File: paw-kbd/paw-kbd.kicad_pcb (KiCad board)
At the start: 2 copper layers, 30 parts, among them J1 OLED, J2 MJ-4PP-9, SW10 SW_PUSH, SW11 SW_PUSH, SW12 SW_PUSH, SW13 SW_PUSH, SW14 SW_PUSH, SW15 SW_PUSH, SW16 SW_PUSH, SW17 SW_PUSH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

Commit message: schematic
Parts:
- removed D14: DIODE, kbd:D3_TH_SMD
- SW1: renamed from SW4; footprint fp:ChocV1_V2_Hotswap_reversed_choc_spacing -> keeb-footprints:ChocV1_V2_Hotswap_reversed_choc_spacing
- SW10: renamed from SW13; footprint fp:ChocV1_V2_Hotswap_reversed_choc_spacing -> keeb-footprints:ChocV1_V2_Hotswap_reversed_choc_spacing
- SW11: renamed from SW14; footprint fp:ChocV1_V2_Hotswap_reversed_choc_spacing -> keeb-footprints:ChocV1_V2_Hotswap_reversed_choc_spacing
- SW12: renamed from SW15; footprint fp:ChocV1_V2_Hotswap_reversed_choc_spacing -> keeb-footprints:ChocV1_V2_Hotswap_reversed_choc_spacing
- SW13: renamed from SW16; footprint fp:ChocV1_V2_Hotswap_reversed_choc_spacing -> keeb-footprints:ChocV1_V2_Hotswap_reversed_choc_spacing
- SW14: renamed from SW17; footprint fp:ChocV1_V2_Hotswap_reversed_choc_spacing -> keeb-footprints:ChocV1_V2_Hotswap_reversed_choc_spacing
- SW15: renamed from SW18; footprint fp:ChocV1_V2_Hotswap_reversed_choc_spacing -> keeb-footprints:ChocV1_V2_Hotswap_reversed_choc_spacing
- SW2: renamed from SW5; footprint fp:ChocV1_V2_Hotswap_reversed_choc_spacing -> keeb-footprints:ChocV1_V2_Hotswap_reversed_choc_spacing
- SW3: renamed from SW6; footprint fp:ChocV1_V2_Hotswap_reversed_choc_spacing -> keeb-footprints:ChocV1_V2_Hotswap_reversed_choc_spacing
- SW4: renamed from SW7; footprint fp:ChocV1_V2_Hotswap_reversed_choc_spacing -> keeb-footprints:ChocV1_V2_Hotswap_reversed_choc_spacing
- SW5: renamed from SW8; footprint fp:ChocV1_V2_Hotswap_reversed_choc_spacing -> keeb-footprints:ChocV1_V2_Hotswap_reversed_choc_spacing
- SW6: renamed from SW9; footprint fp:ChocV1_V2_Hotswap_reversed_choc_spacing -> keeb-footprints:ChocV1_V2_Hotswap_reversed_choc_spacing
- SW7: renamed from SW10; footprint fp:ChocV1_V2_Hotswap_reversed_choc_spacing -> keeb-footprints:ChocV1_V2_Hotswap_reversed_choc_spacing
- SW8: renamed from SW11; footprint fp:ChocV1_V2_Hotswap_reversed_choc_spacing -> keeb-footprints:ChocV1_V2_Hotswap_reversed_choc_spacing
- SW9: renamed from SW12; footprint fp:ChocV1_V2_Hotswap_reversed_choc_spacing -> keeb-footprints:ChocV1_V2_Hotswap_reversed_choc_spacing
- moved J2 10.9 mm to (203.8, 102.5), turned to -90 degrees
- moved SW4 10.7 mm to (116.7, 64.9), turned to 6 degrees
- moved SW10 10.6 mm to (157.2, 64.0), turned to 0 degrees
- moved SW13 10.6 mm to (175.3, 64.0), turned to 0 degrees
- moved SW7 10.6 mm to (136.8, 61.0), turned to 3 degrees
- moved U1 10.5 mm to (194.1, 75.9), turned to 0 degrees
- moved SW5 9.78 mm to (118.5, 82.0), turned to 6 degrees
- moved SW11 9.75 mm to (157.2, 81.1), turned to 0 degrees
- moved SW14 9.70 mm to (175.3, 81.1), turned to 0 degrees
- moved SW8 9.67 mm to (137.7, 78.2), turned to 3 degrees
- moved JP4 9.65 mm to (197.0, 91.6), turned to -90 degrees
- moved JP5 9.65 mm to (197.0, 91.6), turned to -90 degrees
- moved JP3 9.64 mm to (195.1, 91.6), turned to -90 degrees
- moved JP6 9.64 mm to (195.1, 91.6), turned to -90 degrees
- moved JP2 9.63 mm to (193.2, 91.6), turned to -90 degrees
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- renumbered JP4 to JP1, JP3 to JP2, JP2 to JP3, JP1 to JP4, SW22 to SW16, SW22 to SW17

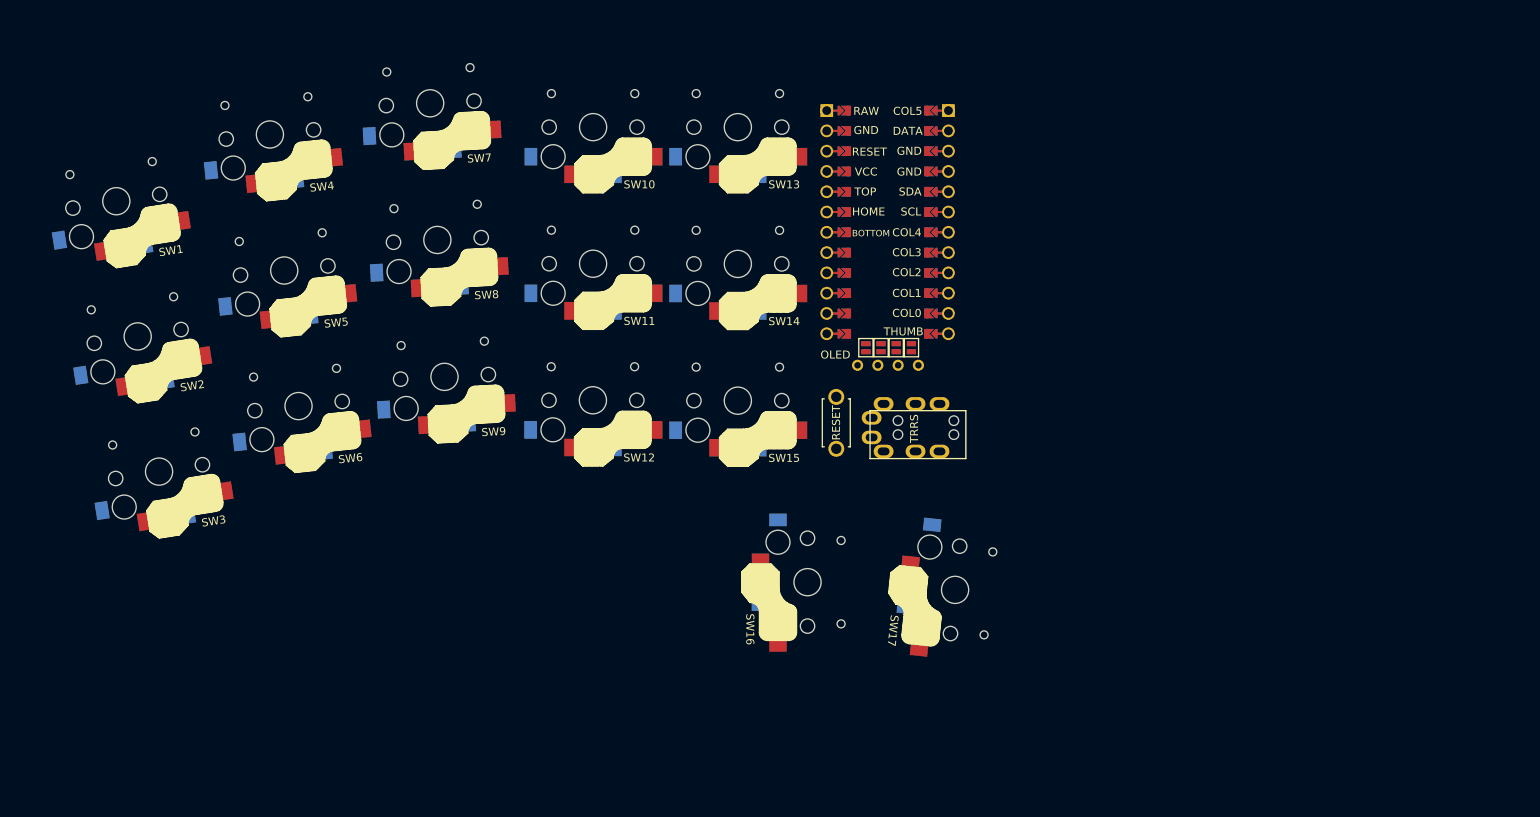
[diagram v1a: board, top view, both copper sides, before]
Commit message: optional socketed footprints
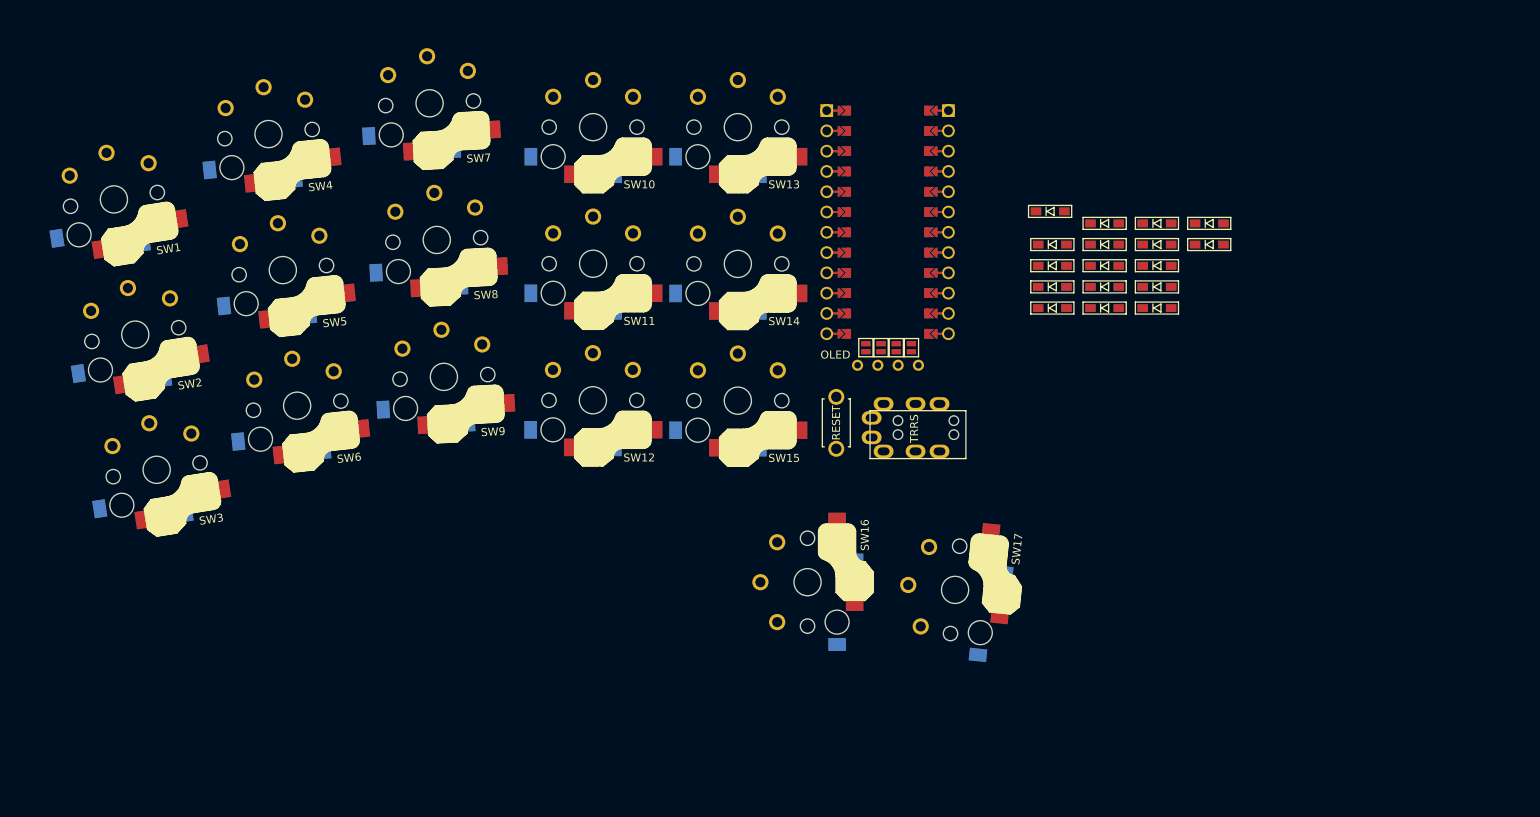
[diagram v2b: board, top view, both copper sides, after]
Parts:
- added D1: DIODE, keeb-footprints:D3_SMD, F.Cu at (214.7, 78.7)
- added D10: DIODE, keeb-footprints:D3_SMD, F.Cu at (214.7, 86.7)
- added D11: DIODE, keeb-footprints:D3_SMD, F.Cu at (221.2, 86.7)
- added D12: DIODE, keeb-footprints:D3_SMD, F.Cu at (227.8, 81.4)
- added D13: DIODE, keeb-footprints:D3_SMD, F.Cu at (227.8, 84.0)
- added D14: DIODE, keeb-footprints:D3_SMD, F.Cu at (221.2, 84.0)
- added D15: DIODE, keeb-footprints:D3_SMD, F.Cu at (234.3, 76.1)
- added D16: DIODE, keeb-footprints:D3_SMD, F.Cu at (227.8, 86.7)
- added D17: DIODE, keeb-footprints:D3_SMD, F.Cu at (227.8, 76.1)
- added D2: DIODE, keeb-footprints:D3_SMD, F.Cu at (214.7, 84.0)
- added D3: DIODE, keeb-footprints:D3_SMD, F.Cu at (234.3, 78.7)
- added D4: DIODE, keeb-footprints:D3_SMD, F.Cu at (221.2, 78.7)
- added D5: DIODE, keeb-footprints:D3_SMD, F.Cu at (214.4, 74.6)
- added D6: DIODE, keeb-footprints:D3_SMD, F.Cu at (221.2, 81.4)
- added D7: DIODE, keeb-footprints:D3_SMD, F.Cu at (227.8, 78.7)
- added D8: DIODE, keeb-footprints:D3_SMD, F.Cu at (221.2, 76.1)
- added D9: DIODE, keeb-footprints:D3_SMD, F.Cu at (214.7, 81.4)
- SW1, SW10, SW11, SW12, SW13, SW14, SW15, SW2, SW3, SW4, SW5, SW6, SW7, SW8, SW9: footprint keeb-footprints:ChocV1_V2_Hotswap_reversed_choc_spacing -> keeb-footprints:ChocV1_V2_Hotswap_optional_reversed_choc_spacing
- SW16, SW17: footprint fp:ChocV1_V2_Hotswap_reversed_15u_choc_spacing -> keeb-footprints:ChocV1_V2_Hotswap_optional_reversed_15u_choc_spacing
- U1: footprint fp:ProMicro_unrouted_type_c -> keeb-footprints:ProMicro_unrouted_type_c
- moved SW3 0.38 mm to (102.5, 106.9)
- moved SW2 0.38 mm to (99.8, 90.0)
- moved SW1 0.38 mm to (97.2, 73.1)
- moved SW4 0.18 mm to (116.5, 64.9)
- moved SW5 0.18 mm to (118.3, 81.9)
- moved SW6 0.18 mm to (120.1, 98.9)
- moved SW7 0.07 mm to (136.7, 61.0)
- moved SW8 0.07 mm to (137.6, 78.2)
- moved SW9 0.07 mm to (138.5, 95.3)
- turned SW16 to 90 degrees
- turned SW17 to 84 degrees
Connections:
- J1 pad 1: (no net) -> Net-(J1-Pad1)
- J1 pad 2: (no net) -> Net-(J1-Pad2)
- J1 pad 3: (no net) -> Net-(J1-Pad3)
- J1 pad 4: (no net) -> Net-(J1-Pad4)
- J2 pad A: (no net) -> GND
- J2 pad B: (no net) -> GND
- J2 pad C: (no net) -> data
- J2 pad D: (no net) -> VCC
- JP1 pad 1: (no net) -> GND
- JP1 pad 2: (no net) -> Net-(J1-Pad4)
- JP2 pad 1: (no net) -> VCC
- JP2 pad 2: (no net) -> Net-(J1-Pad3)
- JP3 pad 1: (no net) -> SCL
- JP3 pad 2: (no net) -> Net-(J1-Pad2)
- JP4 pad 1: (no net) -> SDA
- JP4 pad 2: (no net) -> Net-(J1-Pad1)
- JP5 pad 1: (no net) -> SDA
- JP5 pad 2: (no net) -> Net-(J1-Pad4)
- JP6 pad 1: (no net) -> SCL
- JP6 pad 2: (no net) -> Net-(J1-Pad3)
- JP7 pad 1: (no net) -> VCC
- JP7 pad 2: (no net) -> Net-(J1-Pad2)
- JP8 pad 1: (no net) -> GND
- JP8 pad 2: (no net) -> Net-(J1-Pad1)
- RSW1 pad 1: (no net) -> reset
- RSW1 pad 2: (no net) -> GND
- SW1 pad 1: (no net) -> col1
- SW1 pad 2: (no net) -> Net-(D1-Pad1)
- SW10 pad 1: (no net) -> col4
- SW10 pad 2: (no net) -> Net-(D10-Pad1)
- SW11 pad 1: (no net) -> col4
- SW11 pad 2: (no net) -> Net-(D11-Pad1)
- SW12 pad 1: (no net) -> col4
- SW12 pad 2: (no net) -> Net-(D12-Pad1)
- SW13 pad 1: (no net) -> col5
- SW13 pad 2: (no net) -> Net-(D13-Pad1)
- SW14 pad 1: (no net) -> col5
- SW14 pad 2: (no net) -> Net-(D14-Pad1)
- SW15 pad 1: (no net) -> col5
- SW15 pad 2: (no net) -> Net-(D15-Pad1)
- SW16 pad 1: (no net) -> col4
- SW16 pad 2: (no net) -> Net-(D16-Pad1)
- SW17 pad 1: (no net) -> col5
- SW17 pad 2: (no net) -> Net-(D17-Pad1)
- SW2 pad 1: (no net) -> col1
- SW2 pad 2: (no net) -> Net-(D2-Pad1)
- SW3 pad 1: (no net) -> col1
- SW3 pad 2: (no net) -> Net-(D3-Pad1)
- SW4 pad 1: (no net) -> col2
- SW4 pad 2: (no net) -> Net-(D4-Pad1)
- SW5 pad 1: (no net) -> col2
- SW5 pad 2: (no net) -> Net-(D5-Pad1)
- SW6 pad 1: (no net) -> col2
- SW6 pad 2: (no net) -> Net-(D6-Pad1)
- SW7 pad 1: (no net) -> col3
- SW7 pad 2: (no net) -> Net-(D7-Pad1)
- SW8 pad 1: (no net) -> col3
- SW8 pad 2: (no net) -> Net-(D8-Pad1)
- SW9 pad 1: (no net) -> col3
- SW9 pad 2: (no net) -> Net-(D9-Pad1)
- U1 pad 1: (no net) -> col5
- U1 pad 10: (no net) -> col1
- U1 pad 11: (no net) -> col0
- U1 pad 12: (no net) -> thumb
- U1 pad 13: (no net) -> unconnected-(U1-Pad13)
- U1 pad 14: (no net) -> unconnected-(U1-Pad14)
- U1 pad 15: (no net) -> unconnected-(U1-Pad15)
- U1 pad 16: (no net) -> unconnected-(U1-Pad16)
- U1 pad 17: (no net) -> unconnected-(U1-Pad17)
- U1 pad 18: (no net) -> bottom
- U1 pad 19: (no net) -> home
- U1 pad 2: (no net) -> data
- U1 pad 20: (no net) -> top
- U1 pad 21: (no net) -> VCC
- U1 pad 22: (no net) -> reset
- U1 pad 23: (no net) -> GND
- U1 pad 24: (no net) -> unconnected-(U1-Pad24)
- U1 pad 3: (no net) -> GND
- U1 pad 4: (no net) -> GND
- U1 pad 5: (no net) -> SDA
- U1 pad 6: (no net) -> SCL
- U1 pad 7: (no net) -> col4
- U1 pad 8: (no net) -> col3
- U1 pad 9: (no net) -> col2

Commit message: oval outline
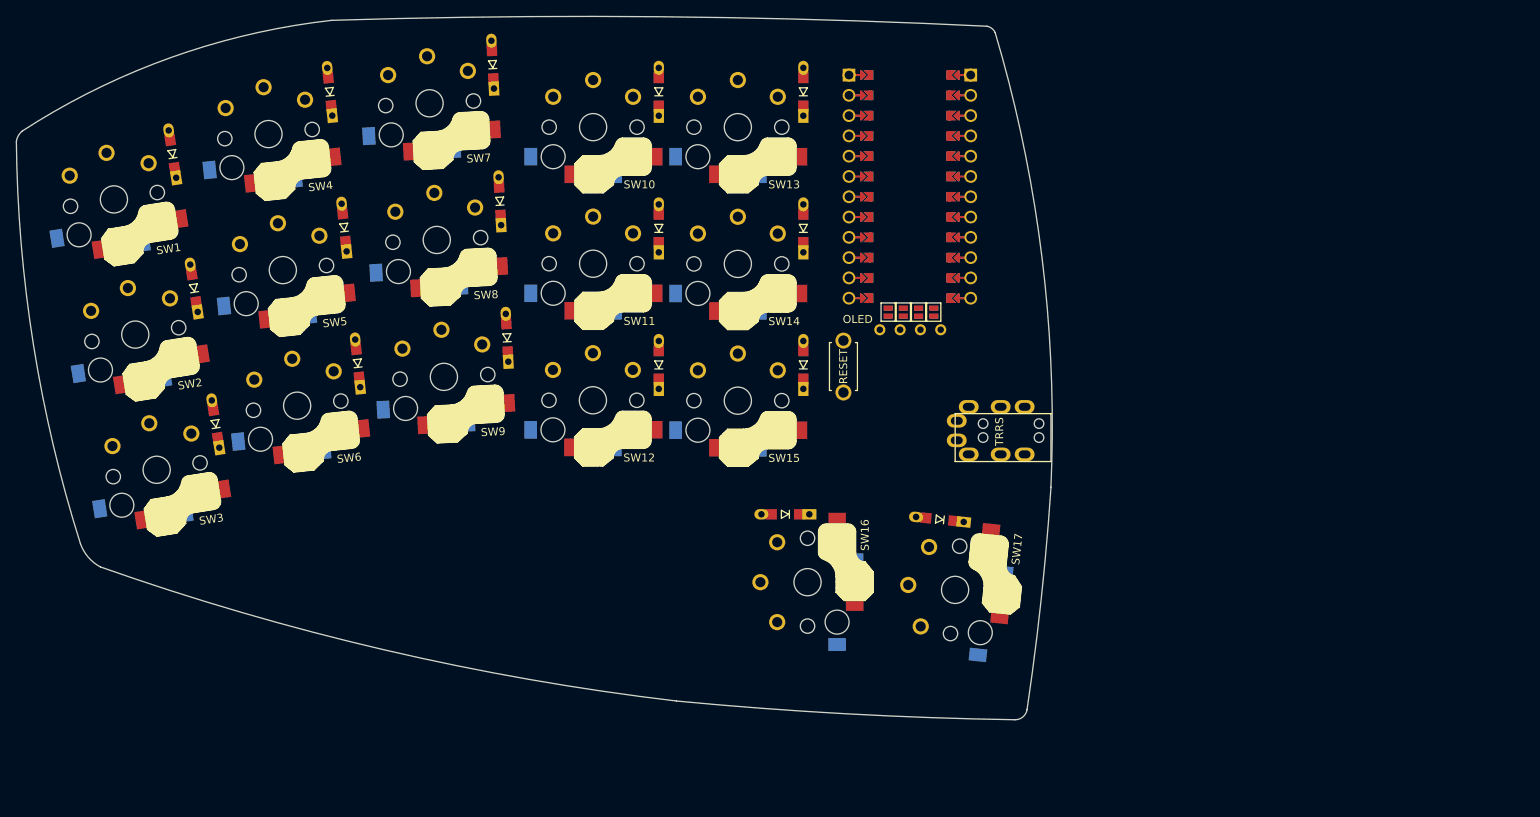
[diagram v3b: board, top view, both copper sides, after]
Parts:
- D1, D10, D11, D12, D13, D14, D15, D16, D17, D2, D3, D4, D5, D6, D7, D8, D9: footprint keeb-footprints:D3_SMD -> kbd:D3_TH_SMD_v2
- moved D3 126.4 mm to (109.9, 101.2), turned to 99 degrees
- moved D1 110.8 mm to (104.5, 67.4), turned to 99 degrees
- moved D2 107.5 mm to (107.2, 84.2), turned to 99 degrees
- moved D4 98.9 mm to (124.2, 59.6), turned to 96 degrees
- moved D6 94.3 mm to (127.7, 93.6), turned to 96 degrees
- moved D5 88.4 mm to (126.0, 76.6), turned to 96 degrees
- moved D7 86.2 mm to (144.6, 56.2), turned to 93 degrees
- moved D8 75.8 mm to (145.5, 73.3), turned to 93 degrees
- moved D9 68.9 mm to (146.4, 90.4), turned to 93 degrees
- moved D12 63.6 mm to (165.4, 93.8), turned to 90 degrees
- moved D11 56.7 mm to (165.4, 76.7), turned to 90 degrees
- moved D10 56.2 mm to (165.4, 59.6), turned to 90 degrees
- moved D15 53.8 mm to (183.5, 93.8), turned to 90 degrees
- moved D16 53.2 mm to (181.2, 112.5), turned to 180 degrees
- moved D13 50.6 mm to (183.5, 59.6), turned to 90 degrees
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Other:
- board outline added: 129.7 x 88.1 mm

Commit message: wip
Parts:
- added BZ1: Buzzer, Buzzer_Beeper:Buzzer_Mallory_AST1109MLTRQ, F.Cu at (137.4, 113.2)
- added J3: TRACKBALL, keeb-footprints:pimoroni, F.Cu at (155.9, 128.8)
- added JP10: Device_Jumper_NO_Small, kbd:Jumper, F.Cu at (157.5, 114.1)
- added JP11: Device_Jumper_NO_Small, kbd:Jumper, F.Cu at (160.9, 117.0)
- added JP12: Device_Jumper_NO_Small, kbd:Jumper, F.Cu at (164.4, 114.1)
- added JP13: Device_Jumper_NO_Small, kbd:Jumper, F.Cu at (164.4, 117.0)
- added JP14: Device_Jumper_NO_Small, kbd:Jumper, F.Cu at (160.9, 114.1)
- added JP9: Device_Jumper_NO_Small, kbd:Jumper, F.Cu at (157.5, 117.0)
- added SW18: RotaryEncoder_Switch, Rotary_Encoder:RotaryEncoder_Alps_EC12E-Switch_Vertical_H20mm, F.Cu at (186.1, 97.5)
- J1: footprint kbd:OLED_v2 -> keeb-footprints:SSD1306_128x64OLED
- J2: value MJ-4PP-9 -> TRRS
- JP5, JP6, JP7, JP8: moved to F.Cu
- RSW1: footprint kbd:ResetSW -> keeb-footprints:SW_Push_1P1T-MP_NO_Horizontal_both_sides
- U1: footprint keeb-footprints:ProMicro_unrouted_type_c -> keeb-footprints:ProMicro_v2
- moved JP7 31.1 mm to (226.9, 90.8), turned to 0 degrees
- moved JP8 29.6 mm to (223.5, 90.8), turned to 0 degrees
- moved JP1 29.4 mm to (223.5, 87.9), turned to 0 degrees
- moved JP3 29.0 mm to (226.9, 87.9), turned to 0 degrees
- moved RSW1 24.8 mm to (213.3, 95.8)
- moved JP6 22.2 mm to (220.1, 87.9), turned to 0 degrees
- moved JP2 20.6 mm to (216.6, 87.9), turned to 0 degrees
- moved JP5 20.6 mm to (220.1, 90.8), turned to 0 degrees
- moved JP4 17.2 mm to (216.6, 90.8), turned to 0 degrees
- moved J1 9.56 mm to (199.5, 80.2), turned to 180 degrees
- moved U1 3.03 mm to (199.3, 73.2)
- moved J2 0.98 mm to (215.1, 103.7)
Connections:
- D13 pad 2: Net-(D1-Pad2) -> thumb
- D14 pad 2: Net-(D11-Pad2) -> Net-(D1-Pad2)
- D15 pad 2: Net-(D12-Pad2) -> Net-(D11-Pad2)
- D16 pad 2: thumb -> Net-(D12-Pad2)
- SW13 pad 2: Net-(D13-Pad1) -> Net-(D14-Pad1)
- SW14 pad 2: Net-(D14-Pad1) -> Net-(D15-Pad1)
- SW15 pad 2: Net-(D15-Pad1) -> Net-(D16-Pad1)
- SW16 pad 2: Net-(D16-Pad1) -> Net-(D13-Pad1)
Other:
- board size 129.7 x 88.1 mm -> 130.8 x 88.1 mm
